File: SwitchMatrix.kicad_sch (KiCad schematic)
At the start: 160 parts, among them SW1 1u, SW10 1u, SW11 1u, SW12 1u, SW13 1u, SW14 1u, SW15 1u, SW16 1u, SW17 2u, SW18 1.5u, SW19 1u, SW2 1u, SW20 1u, SW21 1u, SW22 1u, SW23 1u, SW24 1u, SW25 1u, SW26 1u, SW27 1u, SW28 1u, SW29 1u, SW3 1u, SW30 1u, SW31 1.5u, SW32 ISO Enter, SW33 1u, SW34 1.25u, SW35 1.75u, SW36 1u, SW37 1u, SW38 1u, SW39 1u, SW4 1u, SW40 1u, SW41 1u, SW42 1u, SW43 1u, SW44 1u, SW45 1u, SW46 1u, SW47 2.25u, SW48 1u, SW49 1u, SW5 1u, SW50 2.25u, SW51 1.25u, SW52 1u, SW53 1u, SW54 1u, SW55 1u, SW56 1u, SW57 1u, SW58 1u, SW59 1u, SW6 1u, SW60 1u, SW61 1u, SW62 1u, SW63 1.75u, SW64 1u, SW65 1u, SW66 1.5u, SW67 1u, SW68 1.5u, SW69 7u, SW7 1u, SW70 1.25u, SW71 1.5u, SW72 1u, SW73 1u, SW74 1u, SW75 1.25u, SW76 1.25u, SW77 1.25u, SW78 6.25u, SW79 1.25u, SW8 1u, SW81 3u, SW82 1u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

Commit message: Correct stabs
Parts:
- S1: value MX_stab -> Back; footprint marbastlib-mx:STAB_MX_P_6.25u -> marbastlib-mx:STAB_MX_2u
- S2: value MX_stab -> LShift; footprint marbastlib-mx:STAB_MX_P_6.25u -> marbastlib-mx:STAB_MX_2u
- S3: value MX_stab -> ISO Enter; footprint marbastlib-mx:STAB_MX_P_6.25u -> marbastlib-mx:STAB_MX_2u
- S4: value MX_stab -> 7u Space; footprint marbastlib-mx:STAB_MX_P_6.25u -> marbastlib-mx:STAB_MX_P_7u
- S5: value MX_stab -> 6.25u Space
- S6: value MX_stab -> Left Split Space; footprint marbastlib-mx:STAB_MX_P_6.25u -> marbastlib-mx:STAB_MX_P_2u
- S7: value MX_stab -> Right Split Space; footprint marbastlib-mx:STAB_MX_P_6.25u -> marbastlib-mx:STAB_MX_P_2u
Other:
- moved on the sheet: S4, S5, S6, S7
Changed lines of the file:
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@@
     (pin "2")
   )
-  (symbol (lib_id "marbastlib-mx:MX_stab") (at 147.32 157.48 0) (unit 1)
-    (in_bom yes) (on_board yes) (fields_autoplaced)
-    (property "Reference" "S7" (id 0) (at 153.67 156.0829 0)
+  (symbol (lib_id "marbastlib-mx:MX_stab") (at 149.86 157.48 0) (unit 1)
+    (in_bom yes) (on_board yes) (fields_autoplaced)
+    (property "Reference" "S7" (id 0) (at 156.21 156.0829 0)
       (effects (font (size 1.27 1.27)) (justify left))
     )
-    (property "Value" "MX_stab" (id 1) (at 153.67 158.6229 0)
+    (property "Value" "Right Split Space" (id 1) (at 156.21 158.6229 0)
       (effects (font (size 1.27 1.27)) (justify left))
     )
-    (property "Footprint" "marbastlib-mx:STAB_MX_P_6.25u" (id 2) (at 147.32 157.48 0)
-      (effects (font (size 1.27 1.27)) hide)
-    )
-    (property "Datasheet" "" (id 3) (at 147.32 157.48 0)
+    (property "Footprint" "marbastlib-mx:STAB_MX_P_2u" (id 2) (at 149.86 157.48 0)
+      (effects (font (size 1.27 1.27)) hide)
+    )
+    (property "Datasheet" "" (id 3) (at 149.86 157.48 0)
       (effects (font (size 1.27 1.27)) hide)
     )
@@
       (effects (font (size 1.27 1.27)) (justify left))
     )
-    (property "Value" "MX_stab" (id 1) (at 12.7 110.49 90)
+    (property "Value" "LShift" (id 1) (at 12.7 110.49 90)
       (effects (font (size 1.27 1.27)) (justify left))
     )
-    (property "Footprint" "marbastlib-mx:STAB_MX_P_6.25u" (id 2) (at 22.86 110.49 0)
+    (property "Footprint" "marbastlib-mx:STAB_MX_2u" (id 2) (at 22.86 110.49 0)
       (effects (font (size 1.27 1.27)) hide)
     )
@@
     (pin "2")
   )
-  (symbol (lib_id "marbastlib-mx:MX_stab") (at 147.32 146.05 0) (unit 1)
-    (in_bom yes) (on_board yes) (fields_autoplaced)
-    (property "Reference" "S5" (id 0) (at 153.67 144.6529 0)
+  (symbol (lib_id "marbastlib-mx:MX_stab") (at 149.86 146.05 0) (unit 1)
+    (in_bom yes) (on_board yes) (fields_autoplaced)
+    (property "Reference" "S5" (id 0) (at 156.21 144.6529 0)
       (effects (font (size 1.27 1.27)) (justify left))
     )
-    (property "Value" "MX_stab" (id 1) (at 153.67 147.1929 0)
+    (property "Value" "6.25u Space" (id 1) (at 156.21 147.1929 0)
       (effects (font (size 1.27 1.27)) (justify left))
     )
-    (property "Footprint" "marbastlib-mx:STAB_MX_P_6.25u" (id 2) (at 147.32 146.05 0)
-      (effects (font (size 1.27 1.27)) hide)
-    )
-    (property "Datasheet" "" (id 3) (at 147.32 146.05 0)
+    (property "Footprint" "marbastlib-mx:STAB_MX_P_6.25u" (id 2) (at 149.86 146.05 0)
+      (effects (font (size 1.27 1.27)) hide)
+    )
+    (property "Datasheet" "" (id 3) (at 149.86 146.05 0)
       (effects (font (size 1.27 1.27)) hide)
     )
@@
     (pin "2")
   )
-  (symbol (lib_id "marbastlib-mx:MX_stab") (at 106.68 146.05 0) (unit 1)
-    (in_bom yes) (on_board yes) (fields_autoplaced)
-    (property "Reference" "S4" (id 0) (at 113.03 144.6529 0)
+  (symbol (lib_id "marbastlib-mx:MX_stab") (at 102.87 146.05 0) (unit 1)
+    (in_bom yes) (on_board yes) (fields_autoplaced)
+    (property "Reference" "S4" (id 0) (at 109.22 144.6529 0)
       (effects (font (size 1.27 1.27)) (justify left))
     )
-    (property "Value" "MX_stab" (id 1) (at 113.03 147.1929 0)
+    (property "Value" "7u Space" (id 1) (at 109.22 147.1929 0)
       (effects (font (size 1.27 1.27)) (justify left))
     )
-    (property "Footprint" "marbastlib-mx:STAB_MX_P_6.25u" (id 2) (at 106.68 146.05 0)
-      (effects (font (size 1.27 1.27)) hide)
-    )
-    (property "Datasheet" "" (id 3) (at 106.68 146.05 0)
+    (property "Footprint" "marbastlib-mx:STAB_MX_P_7u" (id 2) (at 102.87 146.05 0)
+      (effects (font (size 1.27 1.27)) hide)
+    )
+    (property "Datasheet" "" (id 3) (at 102.87 146.05 0)
       (effects (font (size 1.27 1.27)) hide)
     )
@@
       (effects (font (size 1.27 1.27)) (justify right))
     )
-    (property "Value" "MX_stab" (id 1) (at 276.86 58.42 90)
-      (effects (font (size 1.27 1.27)) (justify right))
-    )
-    (property "Footprint" "marbastlib-mx:STAB_MX_P_6.25u" (id 2) (at 274.32 57.15 0)
+    (property "Value" "Back" (id 1) (at 276.86 58.42 90)
+      (effects (font (size 1.27 1.27)) (justify right))
+    )
+    (property "Footprint" "marbastlib-mx:STAB_MX_2u" (id 2) (at 274.32 57.15 0)
       (effects (font (size 1.27 1.27)) hide)
     )
@@
       (effects (font (size 1.27 1.27)) (justify right))
     )
-    (property "Value" "MX_stab" (id 1) (at 269.24 76.1999 90)
-      (effects (font (size 1.27 1.27)) (justify right))
-    )
-    (property "Footprint" "marbastlib-mx:STAB_MX_P_6.25u" (id 2) (at 265.43 74.93 0)
+    (property "Value" "ISO Enter" (id 1) (at 269.24 76.1999 90)
+      (effects (font (size 1.27 1.27)) (justify right))
+    )
+    (property "Footprint" "marbastlib-mx:STAB_MX_2u" (id 2) (at 265.43 74.93 0)
       (effects (font (size 1.27 1.27)) hide)
     )
@@
     (pin "2")
   )
-  (symbol (lib_id "marbastlib-mx:MX_stab") (at 106.68 157.48 0) (unit 1)
-    (in_bom yes) (on_board yes) (fields_autoplaced)
-    (property "Reference" "S6" (id 0) (at 113.03 156.0829 0)
+  (symbol (lib_id "marbastlib-mx:MX_stab") (at 102.87 157.48 0) (unit 1)
+    (in_bom yes) (on_board yes) (fields_autoplaced)
+    (property "Reference" "S6" (id 0) (at 109.22 156.0829 0)
       (effects (font (size 1.27 1.27)) (justify left))
     )
-    (property "Value" "MX_stab" (id 1) (at 113.03 158.6229 0)
+    (property "Value" "Left Split Space" (id 1) (at 109.22 158.6229 0)
       (effects (font (size 1.27 1.27)) (justify left))
     )
-    (property "Footprint" "marbastlib-mx:STAB_MX_P_6.25u" (id 2) (at 106.68 157.48 0)
-      (effects (font (size 1.27 1.27)) hide)
-    )
-    (property "Datasheet" "" (id 3) (at 106.68 157.48 0)
-      (effects (font (size 1.27 1.27)) hide)
-    )
+    (property "Footprint" "marbastlib-mx:STAB_MX_P_2u" (id 2) (at 102.87 157.48 0)
+      (effects (font (size 1.27 1.27)) hide)
+    )
+    (property "Datasheet" "" (id 3) (at 102.87 157.48 0)
+      (effects (font (size 1.27 1.27)) hide)
+    )

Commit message: oops, forgot ANSI enter
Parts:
- added S8: Enter, marbastlib-mx:STAB_MX_2u, symbol marbastlib-mx:MX_stab
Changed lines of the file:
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@@
     (pin "2")
   )
+  (symbol (lib_id "marbastlib-mx:MX_stab") (at 265.43 88.9 90) (unit 1)
+    (in_bom yes) (on_board yes) (fields_autoplaced)
+    (property "Reference" "S8" (id 0) (at 269.24 87.6299 90)
+      (effects (font (size 1.27 1.27)) (justify right))
+    )
+    (property "Value" "Enter" (id 1) (at 269.24 90.1699 90)
+      (effects (font (size 1.27 1.27)) (justify right))
+    )
+    (property "Footprint" "marbastlib-mx:STAB_MX_2u" (id 2) (at 265.43 88.9 0)
+      (effects (font (size 1.27 1.27)) hide)
+    )
+    (property "Datasheet" "" (id 3) (at 265.43 88.9 0)
+      (effects (font (size 1.27 1.27)) hide)
+    )
+  )
 )

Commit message: Attempt to use autoplacer plugin
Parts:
- S32: renamed from S3; footprint marbastlib-mx:STAB_MX_2u -> marbastlib-mx:STAB_MX_ISO
- S47: renamed from S8; footprint marbastlib-mx:STAB_MX_2u -> marbastlib-mx:STAB_MX_P_2.25u
- S50: renamed from S2; footprint marbastlib-mx:STAB_MX_2u -> marbastlib-mx:STAB_MX_2.25u
- S81: renamed from S6; footprint marbastlib-mx:STAB_MX_P_2u -> marbastlib-mx:STAB_MX_P_3u
- S83: renamed from S7; footprint marbastlib-mx:STAB_MX_P_2u -> marbastlib-mx:STAB_MX_P_3u
- renumbered S1 to S17, S4 to S69, S5 to S78
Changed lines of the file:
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@@
   (symbol (lib_id "marbastlib-mx:MX_stab") (at 149.86 157.48 0) (unit 1)
     (in_bom yes) (on_board yes) (fields_autoplaced)
-    (property "Reference" "S7" (id 0) (at 156.21 156.0829 0)
+    (property "Reference" "S83" (id 0) (at 156.21 156.0829 0)
       (effects (font (size 1.27 1.27)) (justify left))
     )
@@
       (effects (font (size 1.27 1.27)) (justify left))
     )
-    (property "Footprint" "marbastlib-mx:STAB_MX_P_2u" (id 2) (at 149.86 157.48 0)
+    (property "Footprint" "marbastlib-mx:STAB_MX_P_3u" (id 2) (at 149.86 157.48 0)
       (effects (font (size 1.27 1.27)) hide)
     )
@@
   (symbol (lib_id "marbastlib-mx:MX_stab") (at 22.86 110.49 270) (unit 1)
     (in_bom yes) (on_board yes)
-    (property "Reference" "S2" (id 0) (at 15.24 107.95 90)
+    (property "Reference" "S50" (id 0) (at 15.24 107.95 90)
       (effects (font (size 1.27 1.27)) (justify left))
     )
@@
       (effects (font (size 1.27 1.27)) (justify left))
     )
-    (property "Footprint" "marbastlib-mx:STAB_MX_2u" (id 2) (at 22.86 110.49 0)
+    (property "Footprint" "marbastlib-mx:STAB_MX_2.25u" (id 2) (at 22.86 110.49 0)
       (effects (font (size 1.27 1.27)) hide)
     )
@@
   (symbol (lib_id "marbastlib-mx:MX_stab") (at 149.86 146.05 0) (unit 1)
     (in_bom yes) (on_board yes) (fields_autoplaced)
-    (property "Reference" "S5" (id 0) (at 156.21 144.6529 0)
+    (property "Reference" "S78" (id 0) (at 156.21 144.6529 0)
       (effects (font (size 1.27 1.27)) (justify left))
     )
@@
   (symbol (lib_id "marbastlib-mx:MX_stab") (at 102.87 146.05 0) (unit 1)
     (in_bom yes) (on_board yes) (fields_autoplaced)
-    (property "Reference" "S4" (id 0) (at 109.22 144.6529 0)
+    (property "Reference" "S69" (id 0) (at 109.22 144.6529 0)
       (effects (font (size 1.27 1.27)) (justify left))
     )
@@
   (symbol (lib_id "marbastlib-mx:MX_stab") (at 274.32 57.15 90) (unit 1)
     (in_bom yes) (on_board yes)
-    (property "Reference" "S1" (id 0) (at 276.86 55.88 90)
+    (property "Reference" "S17" (id 0) (at 276.86 55.88 90)
       (effects (font (size 1.27 1.27)) (justify right))
     )
@@
   (symbol (lib_id "marbastlib-mx:MX_stab") (at 265.43 74.93 90) (unit 1)
     (in_bom yes) (on_board yes) (fields_autoplaced)
-    (property "Reference" "S3" (id 0) (at 269.24 73.6599 90)
+    (property "Reference" "S32" (id 0) (at 269.24 73.6599 90)
       (effects (font (size 1.27 1.27)) (justify right))
     )
@@
       (effects (font (size 1.27 1.27)) (justify right))
     )
-    (property "Footprint" "marbastlib-mx:STAB_MX_2u" (id 2) (at 265.43 74.93 0)
+    (property "Footprint" "marbastlib-mx:STAB_MX_ISO" (id 2) (at 265.43 74.93 0)
       (effects (font (size 1.27 1.27)) hide)
     )
@@
   (symbol (lib_id "marbastlib-mx:MX_stab") (at 102.87 157.48 0) (unit 1)
     (in_bom yes) (on_board yes) (fields_autoplaced)
-    (property "Reference" "S6" (id 0) (at 109.22 156.0829 0)
+    (property "Reference" "S81" (id 0) (at 109.22 156.0829 0)
       (effects (font (size 1.27 1.27)) (justify left))
     )
@@
       (effects (font (size 1.27 1.27)) (justify left))
     )
-    (property "Footprint" "marbastlib-mx:STAB_MX_P_2u" (id 2) (at 102.87 157.48 0)
+    (property "Footprint" "marbastlib-mx:STAB_MX_P_3u" (id 2) (at 102.87 157.48 0)
       (effects (font (size 1.27 1.27)) hide)
     )
@@
   (symbol (lib_id "marbastlib-mx:MX_stab") (at 265.43 88.9 90) (unit 1)
     (in_bom yes) (on_board yes) (fields_autoplaced)
-    (property "Reference" "S8" (id 0) (at 269.24 87.6299 90)
+    (property "Reference" "S47" (id 0) (at 269.24 87.6299 90)
       (effects (font (size 1.27 1.27)) (justify right))
     )
@@
       (effects (font (size 1.27 1.27)) (justify right))
     )
-    (property "Footprint" "marbastlib-mx:STAB_MX_2u" (id 2) (at 265.43 88.9 0)
-      (effects (font (size 1.27 1.27)) hide)
-    )
+    (property "Footprint" "marbastlib-mx:STAB_MX_P_2.25u" (id 2) (at 265.43 88.9 0)
+      (effects (font (size 1.27 1.27)) hide)
+    )

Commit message: even more desperate attempts at autopicker
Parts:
- removed SW82: 1u, marbastlib-mx:SW_MX_1u, symbol marbastlib-mx:MX_SW_solder
- renumbered D70 to D64, D64 to D65, D71 to D66, D65 to D67, D66 to D68, D67 to D69, D68 to D70, D69 to D71, S81 to S69, S69 to S70, S83 to S71, S78 to S80, SW75 to SW67, SW67 to SW68, SW76 to SW69, SW68 to SW70, SW77 to SW71, SW81 to SW72, SW69 to SW73, SW78 to SW74, SW83 to SW75, SW70 to SW76, SW71 to SW77, SW79 to SW78, SW72 to SW79, SW73 to SW80, SW74 to SW81

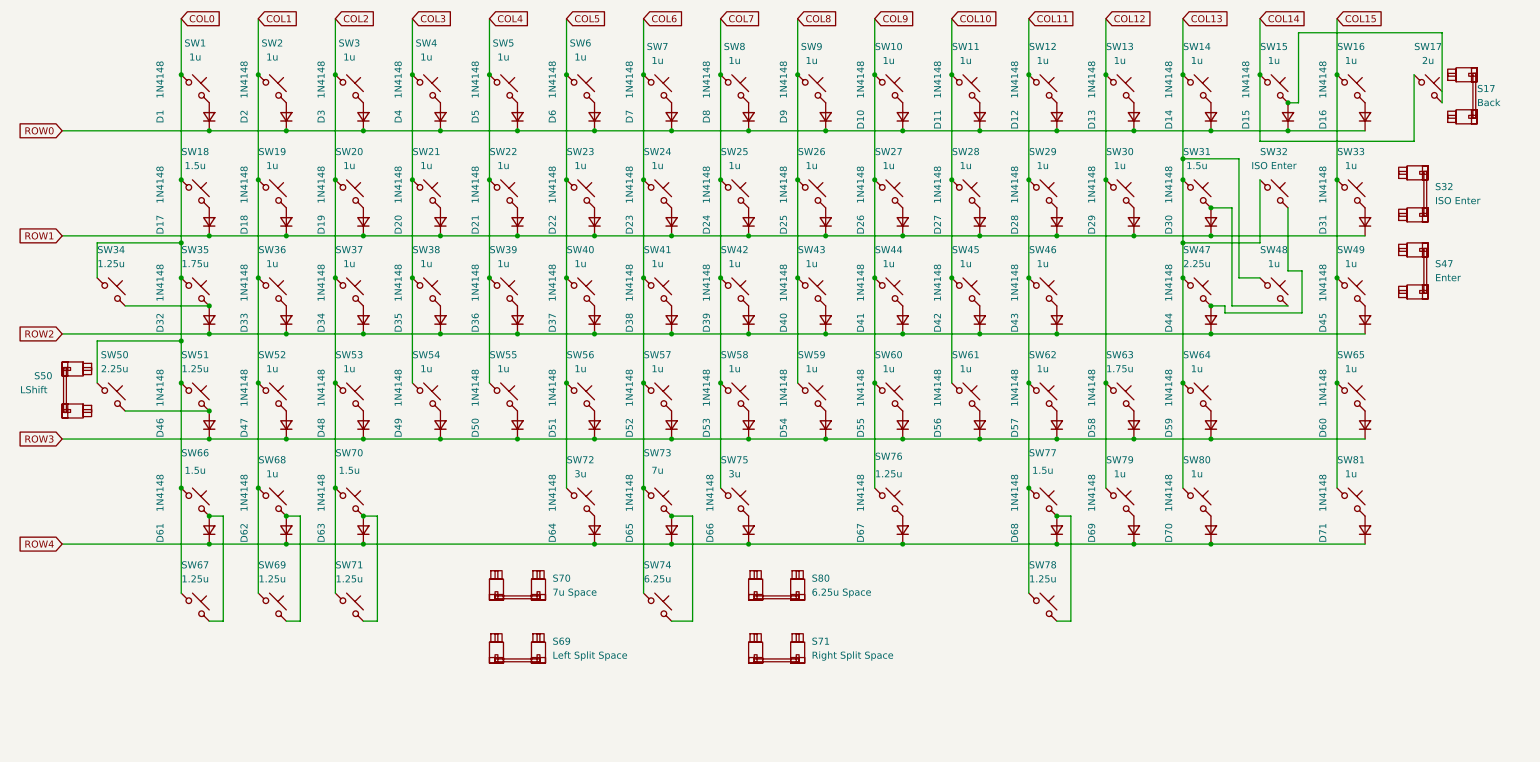
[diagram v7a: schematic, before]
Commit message: Finally got the keys and diodes placed
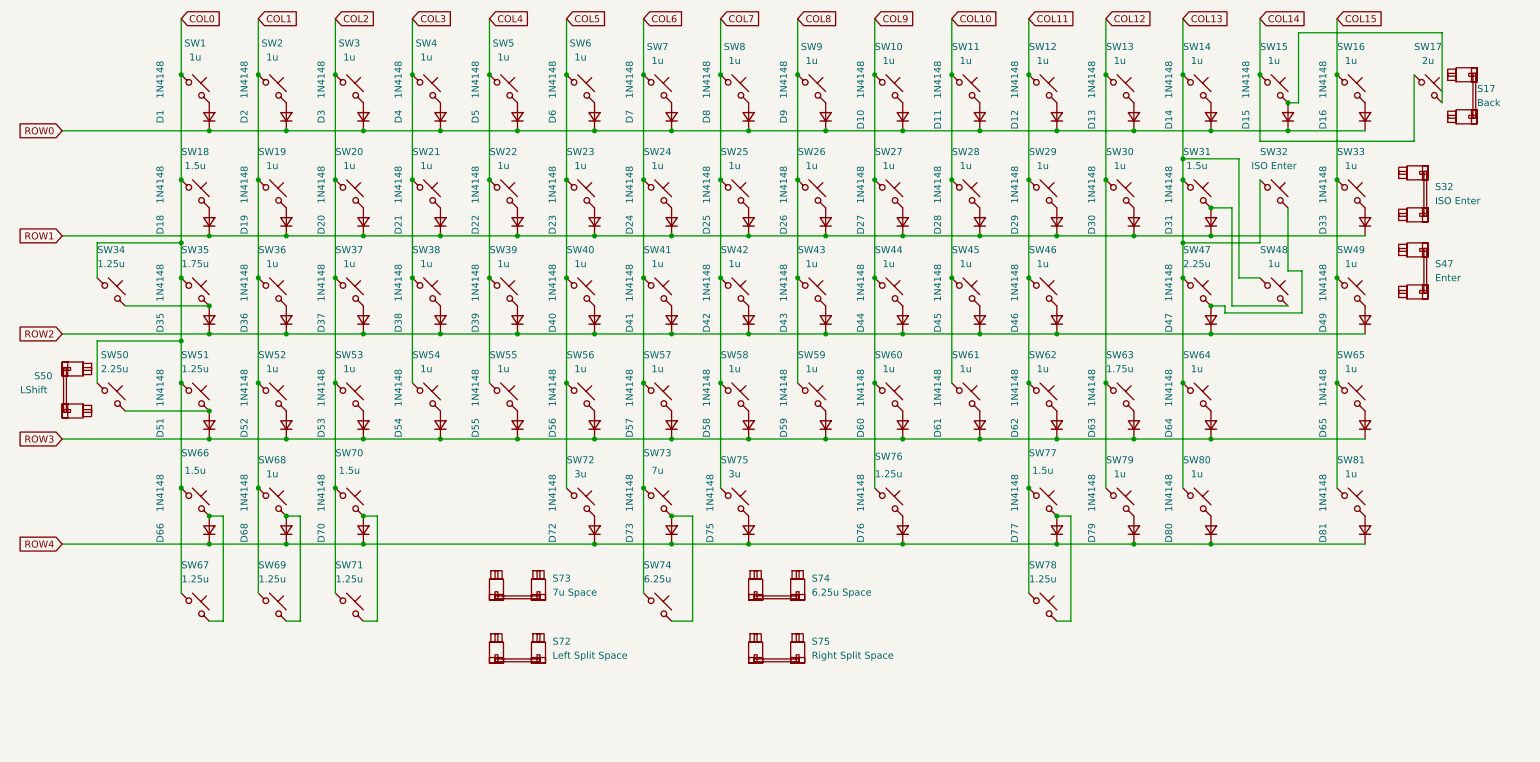
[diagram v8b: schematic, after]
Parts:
- renumbered D17 to D18, D18 to D19, D19 to D20, D20 to D21, D21 to D22, D22 to D23, D23 to D24, D24 to D25, D25 to D26, D26 to D27, D27 to D28, D28 to D29, D29 to D30, D30 to D31, D31 to D33, D32 to D35, D33 to D36, D34 to D37, D35 to D38, D36 to D39, D37 to D40, D38 to D41, D39 to D42, D40 to D43, D41 to D44, D42 to D45, D43 to D46, D44 to D47, D45 to D49, D46 to D51, D47 to D52, D48 to D53, D49 to D54, D50 to D55, D51 to D56, D52 to D57, D53 to D58, D54 to D59, D55 to D60, D56 to D61, D57 to D62, D58 to D63, D59 to D64, D60 to D65, D61 to D66, D62 to D68, D63 to D70, D64 to D72, D65 to D73, D66 to D75, D67 to D76, D68 to D77, D69 to D79, D70 to D80, D71 to D81, S69 to S72, S70 to S73, S80 to S74, S71 to S75
